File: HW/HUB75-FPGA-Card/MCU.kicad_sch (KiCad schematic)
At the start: 2 parts, among them U11 W25Q128JVS, U14 RP2040

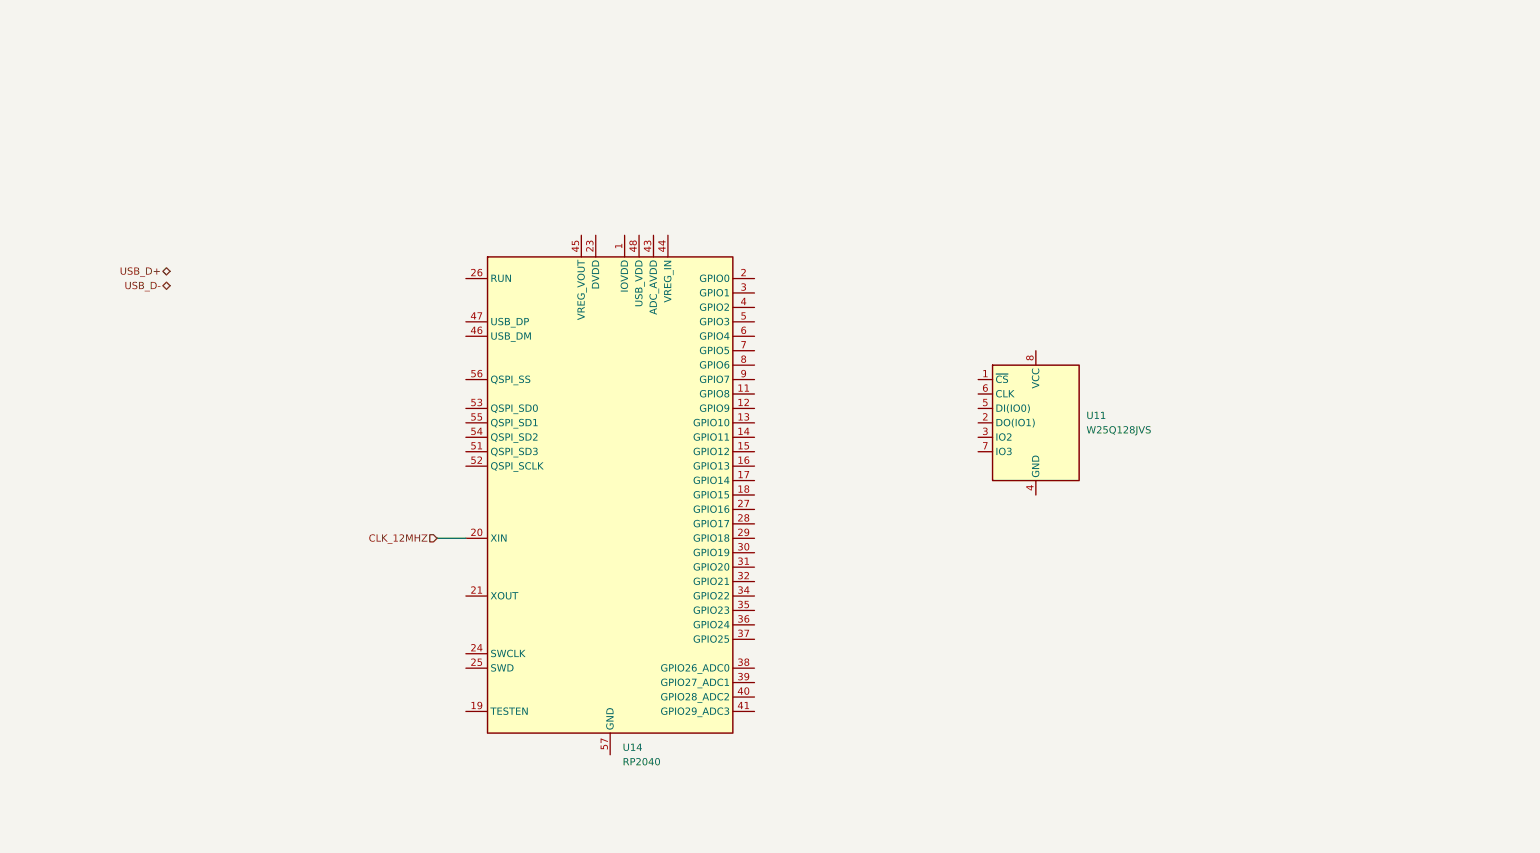
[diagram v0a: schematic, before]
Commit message: initial v1.1 board layout
still needs rp2040 pins routed
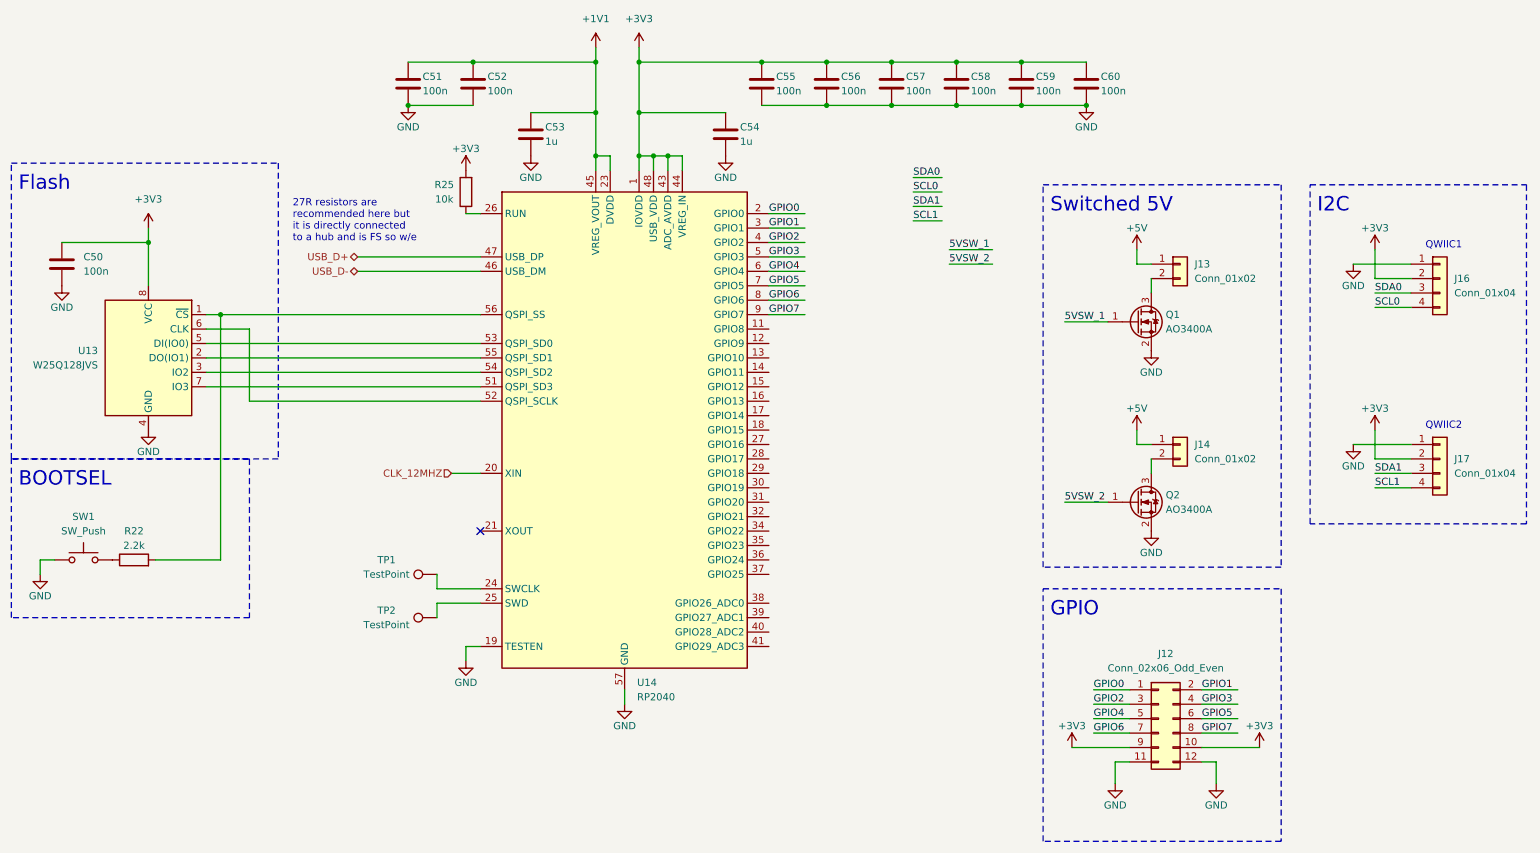
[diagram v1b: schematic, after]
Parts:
- added C50, C51, C52, C55, C56, C57, C58, C59, C60: 100n, Capacitor_SMD:C_0603_1608Metric, symbol Device:C
- added C53, C54: 1u, Capacitor_SMD:C_0603_1608Metric, symbol Device:C
- added J12: Conn_02x06_Odd_Even, Connector_PinHeader_2.54mm:PinHeader_2x06_P2.54mm_Vertical, symbol Connector_Generic:Conn_02x06_Odd_Even
- added J13, J14: Conn_01x02, Connector_PinHeader_2.54mm:PinHeader_1x02_P2.54mm_Vertical, symbol Connector_Generic:Conn_01x02
- added J16, J17: Conn_01x04, Connector_JST:JST_SH_BM04B-SRSS-TB_1x04-1MP_P1.00mm_Vertical, symbol Connector_Generic:Conn_01x04
- added Q1, Q2: AO3400A, Package_TO_SOT_SMD:SOT-23, symbol Transistor_FET:AO3400A
- added R22: 2.2k, Resistor_SMD:R_0603_1608Metric, symbol Device:R
- added R25: 10k, Resistor_SMD:R_0603_1608Metric, symbol Device:R
- added SW1: SW_Push, Project:SW_TS-1187A-B-A-B, symbol Switch:SW_Push
- added TP1, TP2: TestPoint, TestPoint:TestPoint_Pad_D1.0mm, symbol Connector:TestPoint
- renumbered U11 to U13
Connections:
- net USB_D+: now also U14.47 (USB_DP)
- net USB_D-: now also U14.46 (USB_DM)
- net at U13.1 (~{CS}): now also U14.56 (QSPI_SS), R22.2
- net at U13.2 (DO(IO1)): now also U14.55 (QSPI_SD1)
- net at U13.3 (IO2): now also U14.54 (QSPI_SD2)
- net GND: now reaches U13.4 (GND)
- net GND: now also U14.19 (TESTEN), U14.57 (GND), C50.2, C51.2, C52.2, C53.2, C54.2, C55.2, C56.2, C57.2, C58.2, C59.2, C60.2, J12.11 (Pin_11), J12.12 (Pin_12), J16.1 (Pin_1), J17.1 (Pin_1), Q1.2 (S), Q2.2 (S), SW1.1
- net at U13.5 (DI(IO0)): now also U14.53 (QSPI_SD0)
- net at U13.6 (CLK): now also U14.52 (QSPI_SCLK)
- net at U13.7 (IO3): now also U14.51 (QSPI_SD3)
- net +3V3: now reaches U13.8 (VCC)
- net +3V3: now also U14.1 (IOVDD), U14.10 (IOVDD), U14.22 (IOVDD), U14.33 (IOVDD), U14.42 (IOVDD), U14.43 (ADC_AVDD), U14.44 (VREG_IN), U14.48 (USB_VDD), U14.49 (IOVDD), C50.1, C54.1, C55.1, C56.1, C57.1, C58.1, C59.1, C60.1, J12.10 (Pin_10), J12.9 (Pin_9), J16.2 (Pin_2), J17.2 (Pin_2), R25.2
- net GPIO0: now reaches U14.2 (GPIO0)
- net GPIO0: now also J12.1 (Pin_1)
- net +1V1: now reaches U14.23 (DVDD), U14.50 (DVDD)
- net +1V1: now also U14.45 (VREG_VOUT), C51.1, C52.1, C53.1
- net at U14.24 (SWCLK): now also TP1.1
- net at U14.25 (SWD): now also TP2.1
- net at U14.26 (RUN): now also R25.1
- net GPIO1: now reaches U14.3 (GPIO1)
- net GPIO1: now also J12.2 (Pin_2)
- net GPIO2: now reaches U14.4 (GPIO2)
- net GPIO2: now also J12.3 (Pin_3)
- net GPIO3: now reaches U14.5 (GPIO3)
- net GPIO3: now also J12.4 (Pin_4)
- net GPIO4: now reaches U14.6 (GPIO4)
- net GPIO4: now also J12.5 (Pin_5)
- net GPIO5: now reaches U14.7 (GPIO5)
- net GPIO5: now also J12.6 (Pin_6)
- net GPIO6: now reaches U14.8 (GPIO6)
- net GPIO6: now also J12.7 (Pin_7)
- net GPIO7: now reaches U14.9 (GPIO7)
- net GPIO7: now also J12.8 (Pin_8)
- new net: R22.1, SW1.2
- new net: J14.2 (Pin_2), Q2.3 (D)
- new net: J13.2 (Pin_2), Q1.3 (D)
- new net +5V: J13.1 (Pin_1), J14.1 (Pin_1)
- new net 5VSW_1: Q1.1 (G)
- new net 5VSW_2: Q2.1 (G)
- new net SCL0: J16.4 (Pin_4)
- new net SCL1: J17.4 (Pin_4)
- new net SDA0: J16.3 (Pin_3)
- new net SDA1: J17.3 (Pin_3)
- no-connect marks 0 -> 1
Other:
- note added: "27R resistors are recommended here but it is directly connected to a hub and is FS so w/e"
- note added: "BOOTSEL"
- note added: "Flash"
- note added: "GPIO"
- note added: "I2C"
- note added: "QWIIC1"
- note added: "QWIIC2"
- note added: "Switched 5V"
- moved on the sheet: U13, U14

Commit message: finish rp2040 routing
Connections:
- net 5VSW_1: now also U14.8 (GPIO6)
- net 5VSW_2: now also U14.9 (GPIO7)
- net SCL0: now also U14.12 (GPIO9)
- net SCL1: now also U14.18 (GPIO15)
- net SDA0: now also U14.11 (GPIO8)
- net SDA1: now also U14.17 (GPIO14)
- net GPIO26: now reaches U14.38 (GPIO26_ADC0)
- net GPIO26: now also J12.7 (Pin_7)
- net GPIO27: now reaches U14.39 (GPIO27_ADC1)
- net GPIO27: now also J12.8 (Pin_8)
- removed net GPIO6: J12.7 (Pin_7), U14.8 (GPIO6)
- removed net GPIO7: J12.8 (Pin_8), U14.9 (GPIO7)
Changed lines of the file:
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@@
     (stroke (width 0) (type default))
   )
-  (wire (pts (xy 180.34 57.15) (xy 187.96 57.15))
+  (wire (pts (xy 148.59 66.04) (xy 156.21 66.04))
     (stroke (width 0) (type default))
   )
@@
     (stroke (width 0) (type default))
   )
-  (wire (pts (xy 173.99 46.99) (xy 179.07 46.99))
+  (wire (pts (xy 148.59 73.66) (xy 153.67 73.66))
     (stroke (width 0) (type default))
   )
@@
     (stroke (width 0) (type default))
   )
-  (wire (pts (xy 173.99 49.53) (xy 179.07 49.53))
+  (wire (pts (xy 148.59 86.36) (xy 153.67 86.36))
     (stroke (width 0) (type default))
   )
@@
     (stroke (width 0) (type default))
   )
-  (wire (pts (xy 180.34 59.69) (xy 187.96 59.69))
+  (wire (pts (xy 148.59 68.58) (xy 156.21 68.58))
     (stroke (width 0) (type default))
   )
@@
     (stroke (width 0) (type default))
   )
-  (wire (pts (xy 148.59 68.58) (xy 154.94 68.58))
+  (wire (pts (xy 148.59 121.92) (xy 154.94 121.92))
     (stroke (width 0) (type default))
   )
@@
     (stroke (width 0) (type default))
   )
-  (wire (pts (xy 173.99 44.45) (xy 179.07 44.45))
+  (wire (pts (xy 148.59 71.12) (xy 153.67 71.12))
     (stroke (width 0) (type default))
   )
@@
     (stroke (width 0) (type default))
   )
-  (wire (pts (xy 148.59 66.04) (xy 154.94 66.04))
+  (wire (pts (xy 148.59 119.38) (xy 154.94 119.38))
     (stroke (width 0) (type default))
   )
@@
     (stroke (width 0) (type default))
   )
-  (wire (pts (xy 173.99 52.07) (xy 179.07 52.07))
+  (wire (pts (xy 148.59 88.9) (xy 153.67 88.9))
     (stroke (width 0) (type default))
   )
@@
     (effects (font (size 1.27 1.27)) (justify left bottom))
   )
-  (label "5VSW_1" (at 180.34 57.15 0) (fields_autoplaced)
+  (label "5VSW_1" (at 148.59 66.04 0) (fields_autoplaced)
     (effects (font (size 1.27 1.27)) (justify left bottom))
   )
@@
     (effects (font (size 1.27 1.27)) (justify left bottom))
   )
-  (label "SDA0" (at 173.99 44.45 0) (fields_autoplaced)
-    (effects (font (size 1.27 1.27)) (justify left bottom))
-  )
-  (label "GPIO7" (at 224.79 142.24 0) (fields_autoplaced)
+  (label "SDA0" (at 148.59 71.12 0) (fields_autoplaced)
+    (effects (font (size 1.27 1.27)) (justify left bottom))
+  )
+  (label "GPIO27" (at 224.79 142.24 0) (fields_autoplaced)
     (effects (font (size 1.27 1.27)) (justify left bottom))
   )
@@
     (effects (font (size 1.27 1.27)) (justify left bottom))
   )
-  (label "SDA1" (at 173.99 49.53 0) (fields_autoplaced)
-    (effects (font (size 1.27 1.27)) (justify left bottom))
-  )
-  (label "SCL0" (at 173.99 46.99 0) (fields_autoplaced)
+  (label "SDA1" (at 148.59 86.36 0) (fields_autoplaced)
+    (effects (font (size 1.27 1.27)) (justify left bottom))
+  )
+  (label "SCL0" (at 148.59 73.66 0) (fields_autoplaced)
     (effects (font (size 1.27 1.27)) (justify left bottom))
   )
@@
     (effects (font (size 1.27 1.27)) (justify left bottom))
   )
-  (label "GPIO6" (at 148.59 66.04 0) (fields_autoplaced)
+  (label "GPIO26" (at 148.59 119.38 0) (fields_autoplaced)
     (effects (font (size 1.27 1.27)) (justify left bottom))
   )
@@
     (effects (font (size 1.27 1.27)) (justify left bottom))
   )
-  (label "5VSW_2" (at 180.34 59.69 0) (fields_autoplaced)
+  (label "5VSW_2" (at 148.59 68.58 0) (fields_autoplaced)
     (effects (font (size 1.27 1.27)) (justify left bottom))
   )
@@
     (effects (font (size 1.27 1.27)) (justify left bottom))
   )
-  (label "GPIO6" (at 205.74 142.24 0) (fields_autoplaced)
+  (label "GPIO26" (at 205.74 142.24 0) (fields_autoplaced)
     (effects (font (size 1.27 1.27)) (justify left bottom))
   )
@@
     (effects (font (size 1.27 1.27)) (justify left bottom))
   )
-  (label "SCL1" (at 173.99 52.07 0) (fields_autoplaced)
+  (label "SCL1" (at 148.59 88.9 0) (fields_autoplaced)
     (effects (font (size 1.27 1.27)) (justify left bottom))
   )
@@
     (effects (font (size 1.27 1.27)) (justify left bottom))
   )
-  (label "GPIO7" (at 148.59 68.58 0) (fields_autoplaced)
-    (effects (font (size 1.27 1.27)) (justify left bottom))
-  )
+  (label "GPIO27" (at 148.59 121.92 0) (fields_autoplaced)
+    (effects (font (size 1.27 1.27)) (justify left bottom))
+  )
